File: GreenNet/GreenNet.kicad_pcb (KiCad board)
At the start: 2 copper layers, 32 parts, among them U1 ESP32-S3-WROOM-1-N16R2, U2 USB_C_Receptacle_12P, U3 USB_C_Receptacle_12P, U4 CP2102N-A02-GQFN28

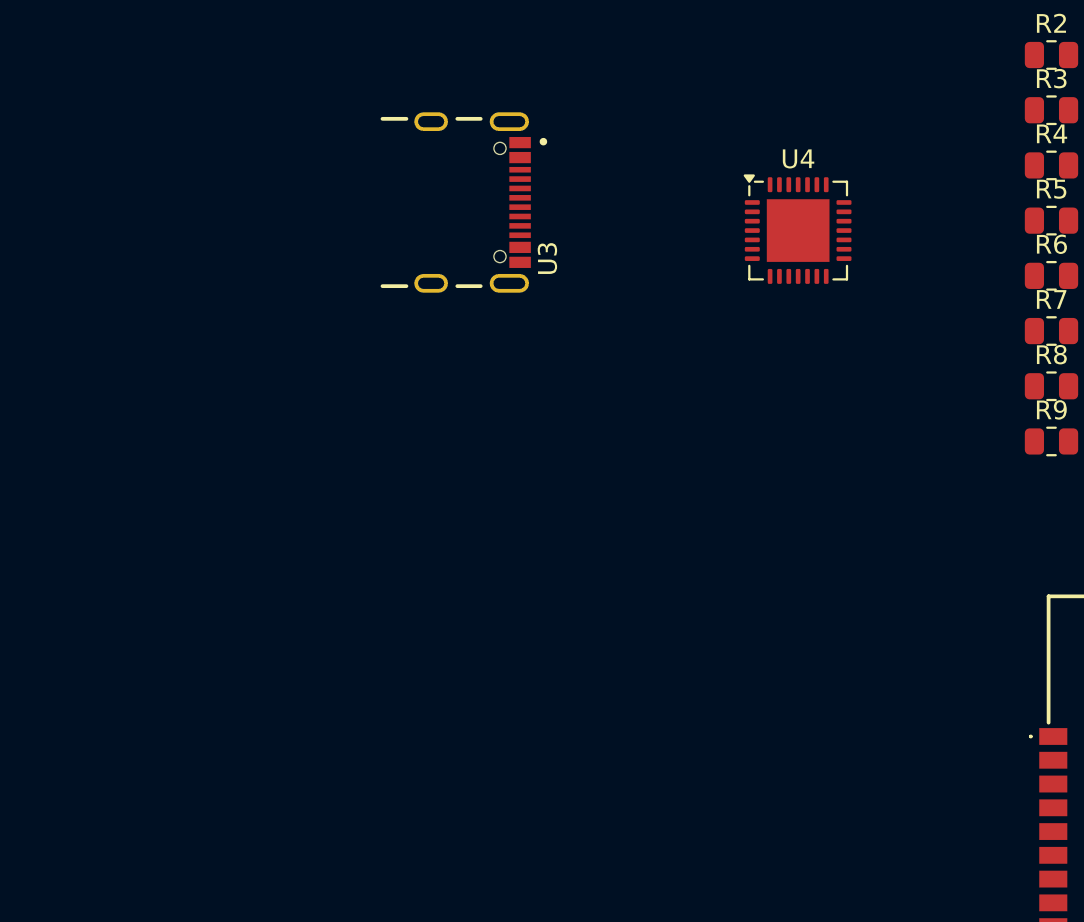
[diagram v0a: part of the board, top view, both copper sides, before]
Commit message: finished input schematic
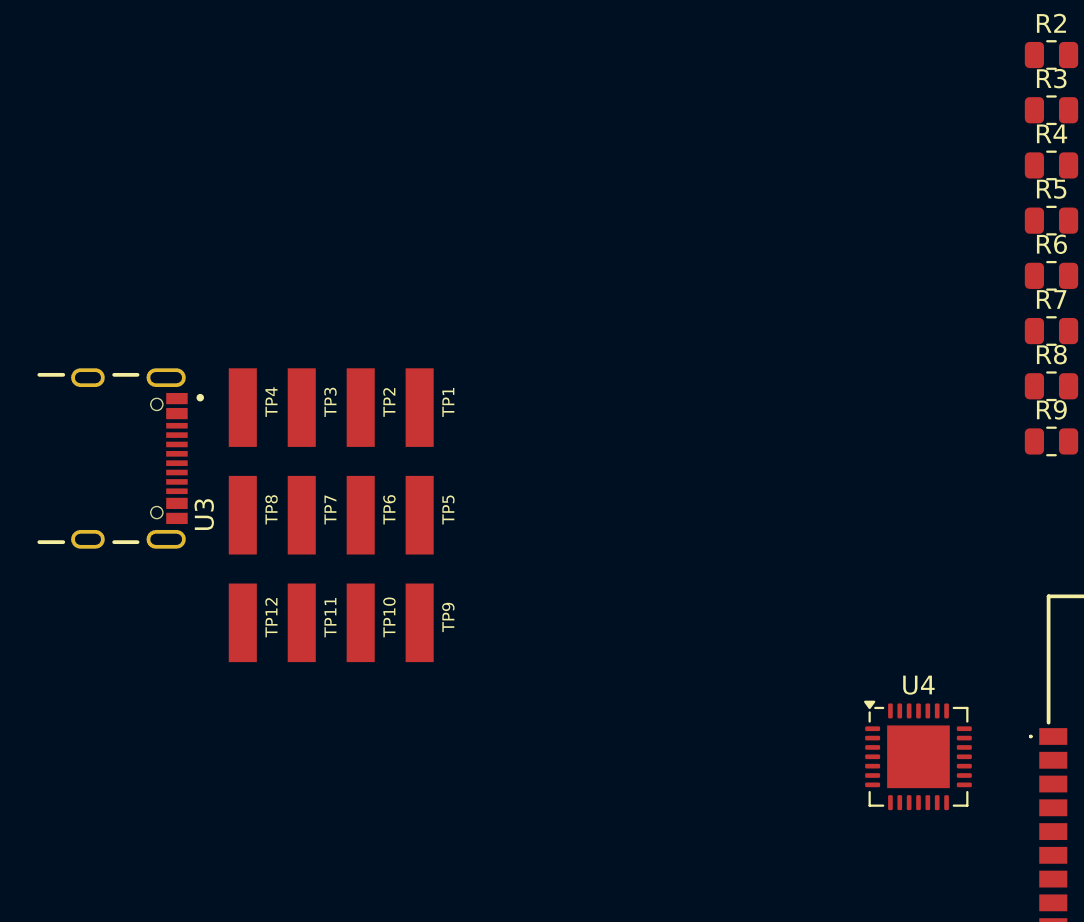
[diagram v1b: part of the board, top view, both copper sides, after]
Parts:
- added TP1: TestPoint, AA_TestPoints:RCWCTE, F.Cu at (103.2, 83.5)
- added TP10: TestPoint, AA_TestPoints:RCWCTE, F.Cu at (100.1, 95.0)
- added TP11: TestPoint, AA_TestPoints:RCWCTE, F.Cu at (96.9, 95.0)
- added TP12: TestPoint, AA_TestPoints:RCWCTE, F.Cu at (93.8, 95.0)
- added TP2: TestPoint, AA_TestPoints:RCWCTE, F.Cu at (100.1, 83.5)
- added TP3: TestPoint, AA_TestPoints:RCWCTE, F.Cu at (96.9, 83.5)
- added TP4: TestPoint, AA_TestPoints:RCWCTE, F.Cu at (93.8, 83.5)
- added TP5: TestPoint, AA_TestPoints:RCWCTE, F.Cu at (103.2, 89.2)
- added TP6: TestPoint, AA_TestPoints:RCWCTE, F.Cu at (100.1, 89.2)
- added TP7: TestPoint, AA_TestPoints:RCWCTE, F.Cu at (96.9, 89.2)
- added TP8: TestPoint, AA_TestPoints:RCWCTE, F.Cu at (93.8, 89.2)
- added TP9: TestPoint, AA_TestPoints:RCWCTE, F.Cu at (103.2, 95.0)
- moved U4 28.8 mm to (129.9, 102.1)
- moved U3 22.9 mm to (85.5, 86.2)
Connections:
- D3 pad 3: /Input/USB_UART_D+ -> /Input/USB_UART_D-
- U3 pad A7: /Input/USB_UART_D+ -> /Input/USB_UART_D-
- U3 pad B7: /Input/USB_UART_D+ -> /Input/USB_UART_D-
- U4 pad 5: /Input/USB_UART_D+ -> /Input/USB_UART_D-

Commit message: MCU fix
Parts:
- added R10: 10k, Resistor_SMD:R_0805_2012Metric, F.Cu at (127.1, 105.5)
- added R11: 10k, Resistor_SMD:R_0805_2012Metric, F.Cu at (127.1, 108.5)
- added U5: MC33063AD, Package_SO:SOIC-8_3.9x4.9mm_P1.27mm, F.Cu at (129.1, 98.8)
- moved R7 73.9 mm to (204.9, 108.5)
- moved D1 68.4 mm to (91.0, 49.1)
- moved D3 67.1 mm to (90.5, 65.1)
- moved U4 66.1 mm to (196.0, 100.5)
- moved D7 63.5 mm to (101.9, 48.6)
- moved C10 58.7 mm to (90.5, 53.6)
- moved D2 58.0 mm to (97.0, 54.6)
- moved R6 56.8 mm to (187.9, 101.5)
- moved D5 55.2 mm to (200.1, 108.5)
- moved D6 55.2 mm to (102.6, 68.1)
- moved U1 54.6 mm to (138.2, 52.3)
- moved D4 51.7 mm to (97.5, 71.6)
- moved C9 51.5 mm to (90.9, 69.6)
- moved C4 51.0 mm to (182.1, 95.5)
- moved C5 51.0 mm to (182.1, 98.5)
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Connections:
- U1 pad 27: unconnected-(U1-IO0-Pad27) -> /Microcontroller/S3_BOOT
- U1 pad 36: unconnected-(U1-RXD0-Pad36) -> /Input/UART_TXD
- U1 pad 37: unconnected-(U1-TXD0-Pad37) -> /Input/UART_RXD
- U1 pad 42: (no net) -> GND
- U1 pad 43: (no net) -> GND
- U1 pad 44: (no net) -> GND
- U1 pad 45: (no net) -> GND
- U1 pad 46: (no net) -> GND
- U1 pad 47: (no net) -> GND
- U1 pad 48: (no net) -> GND
- U1 pad 49: (no net) -> GND
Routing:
- added copper zone on F.Cu, net GND
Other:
- copper layers 2 -> 4

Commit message: USB-PC PD progress
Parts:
- removed R2, R3: 5.1k, Resistor_SMD:R_0805_2012Metric
- removed TP1, TP10, TP11, TP12, TP2, TP3, TP4, TP5, TP6, TP7, TP8, TP9: TestPoint, AA_TestPoints:RCWCTE
- added IC1: BQ24250RGET, QFN:QFN50P400X400X100-25N-D, F.Cu at (132.5, 102.8)
- added Q4: IRF9358TRPBF, AA_FETS:SO8_IRF9358TRPBF_INF, F.Cu at (122.0, 75.6)
- added TP13: TestPoint, AA_TestPoints:RCWCTE, F.Cu at (107.3, 61.2)
- added TP14: TestPoint, AA_TestPoints:RCWCTE, F.Cu at (107.3, 64.4)
- added TP15: TestPoint, AA_TestPoints:RCWCTE, F.Cu at (107.3, 67.5)
- added TP16: TestPoint, AA_TestPoints:RCWCTE, F.Cu at (107.3, 70.7)
- added TP17: TestPoint, AA_TestPoints:RCWCTE, F.Cu at (113.0, 61.2)
- added TP18: TestPoint, AA_TestPoints:RCWCTE, F.Cu at (113.0, 64.4)
- added TP19: TestPoint, AA_TestPoints:RCWCTE, F.Cu at (113.0, 67.5)
- added TP20: TestPoint, AA_TestPoints:RCWCTE, F.Cu at (113.0, 70.7)
- added TP21: TestPoint, AA_TestPoints:RCWCTE, F.Cu at (118.8, 61.2)
- added TP22: TestPoint, AA_TestPoints:RCWCTE, F.Cu at (118.8, 64.4)
- added TP23: TestPoint, AA_TestPoints:RCWCTE, F.Cu at (118.8, 67.5)
- added TP24: TestPoint, AA_TestPoints:RCWCTE, F.Cu at (118.8, 70.7)
- added U6: CYPD3177-24LQXQT, AA_Interface_USB:QFN50P400X400X60-25N-D, F.Cu at (121.2, 89.3)
- moved R7 97.4 mm to (111.0, 82.6)
- moved D8 95.1 mm to (115.5, 82.9)
- moved D9 95.1 mm to (115.5, 86.0)
- moved D5 91.5 mm to (115.5, 73.8)
- moved R6 79.9 mm to (111.0, 79.6)
- moved C4 78.5 mm to (106.6, 73.8)
- moved C5 78.5 mm to (106.6, 76.8)
- moved C6 78.5 mm to (106.6, 79.8)
- moved C7 78.5 mm to (106.6, 82.8)
- moved C8 78.5 mm to (106.6, 85.8)
- moved U4 78.0 mm to (118.0, 99.5)
- moved C10 41.5 mm to (106.6, 91.8)
- moved R10 41.2 mm to (152.6, 73.1)
- moved R11 41.2 mm to (152.6, 76.1)
- moved R9 37.2 mm to (111.0, 88.5)
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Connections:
- R6 pad 1: VDD -> /Input/UART_VDD
- U2 pad A5: Net-(U2-CC1) -> /Input/USB_CC1
- U2 pad B5: Net-(U2-CC2) -> /Input/USB_CC2
- U4 pad 6: VDD -> /Input/UART_VDD
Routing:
- removed copper zone on F.Cu, net GND

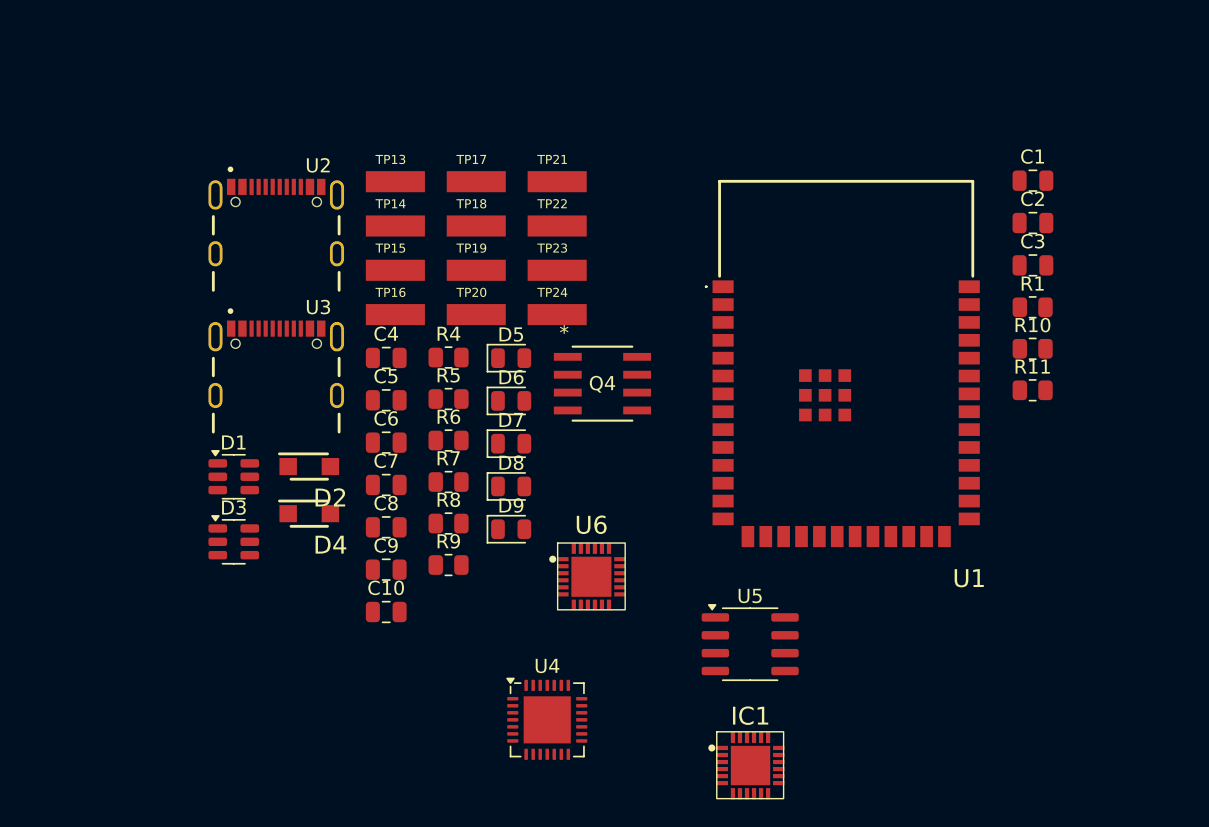
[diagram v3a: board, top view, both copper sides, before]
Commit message: input schematic finished
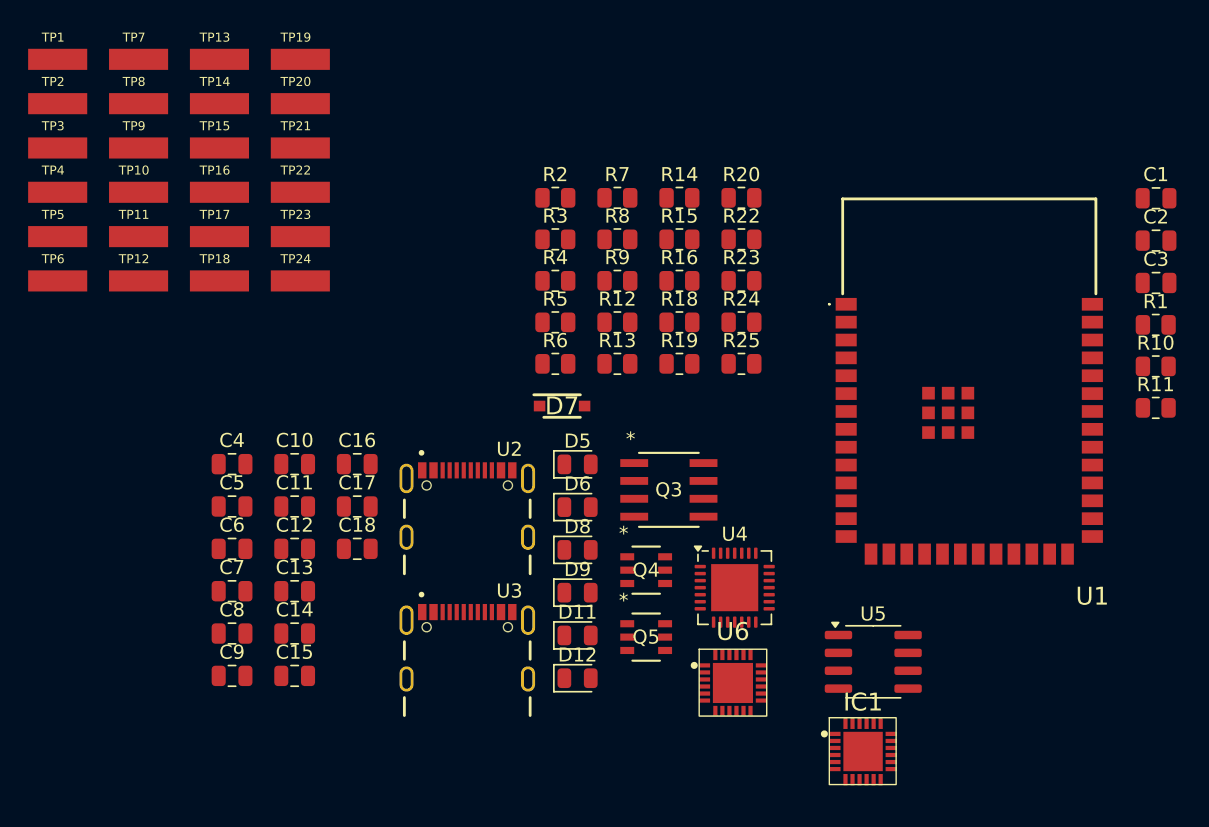
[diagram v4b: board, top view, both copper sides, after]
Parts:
- removed D1, D3: ESDA6V1BC6, Package_TO_SOT_SMD:SOT-23-6
- removed D2, D4: DSS14U, AA_Diodes:SOD-123FL
- added C11: 1u, Capacitor_SMD:C_0805_2012Metric, F.Cu at (100.1, 84.3)
- added C12: 1u, Capacitor_SMD:C_0805_2012Metric, F.Cu at (100.1, 87.3)
- added C13: 0.1u, Capacitor_SMD:C_0805_2012Metric, F.Cu at (100.1, 90.4)
- added C14: 0.1u, Capacitor_SMD:C_0805_2012Metric, F.Cu at (100.1, 93.4)
- added C15: 390p, Capacitor_SMD:C_0805_2012Metric, F.Cu at (100.1, 96.4)
- added C16: 390p, Capacitor_SMD:C_0805_2012Metric, F.Cu at (104.5, 81.3)
- added C17: 1u, Capacitor_SMD:C_0805_2012Metric, F.Cu at (104.5, 84.3)
- added C18: 1u, Capacitor_SMD:C_0805_2012Metric, F.Cu at (104.5, 87.3)
- added D11: Green, LED_SMD:LED_0805_2012Metric, F.Cu at (120.2, 93.5)
- added D12: Red, LED_SMD:LED_0805_2012Metric, F.Cu at (120.2, 96.5)
- added Q3: IRF9358TRPBF, AA_FETS:SO8_IRF9358TRPBF_INF, F.Cu at (126.7, 83.2)
- added Q5: SI3993CDV-T1-GE3, AA_FETS:TSOP_0DV-T1-E3_VIS, F.Cu at (125.1, 93.6)
- added R12: 49.9k, Resistor_SMD:R_0805_2012Metric, F.Cu at (123.0, 71.2)
- added R13: 1k, Resistor_SMD:R_0805_2012Metric, F.Cu at (123.0, 74.2)
- added R14: 49.9k, Resistor_SMD:R_0805_2012Metric, F.Cu at (127.4, 62.4)
- added R15: 62R, Resistor_SMD:R_0805_2012Metric, F.Cu at (127.4, 65.3)
- added R16: 49.9k, Resistor_SMD:R_0805_2012Metric, F.Cu at (127.4, 68.3)
- added R18: 62R, Resistor_SMD:R_0805_2012Metric, F.Cu at (127.4, 71.2)
- added R19: 62R, Resistor_SMD:R_0805_2012Metric, F.Cu at (127.4, 74.2)
- added R2: 1k, Resistor_SMD:R_0805_2012Metric, F.Cu at (118.6, 62.4)
- added R20: 62R, Resistor_SMD:R_0805_2012Metric, F.Cu at (131.9, 62.4)
- added R22: 5.1k, Resistor_SMD:R_0805_2012Metric, F.Cu at (131.9, 65.3)
- added R23: 1k, Resistor_SMD:R_0805_2012Metric, F.Cu at (131.9, 68.3)
- added R24: 5.1k, Resistor_SMD:R_0805_2012Metric, F.Cu at (131.9, 71.2)
- added R25: 2.4k, Resistor_SMD:R_0805_2012Metric, F.Cu at (131.9, 74.2)
- added R3: 10k, Resistor_SMD:R_0805_2012Metric, F.Cu at (118.6, 65.3)
- added TP1: TestPoint, AA_TestPoints:RCWCTE, F.Cu at (83.2, 52.5)
- added TP10: TestPoint, AA_TestPoints:RCWCTE, F.Cu at (89.0, 62.0)
- added TP11: TestPoint, AA_TestPoints:RCWCTE, F.Cu at (89.0, 65.2)
- added TP12: TestPoint, AA_TestPoints:RCWCTE, F.Cu at (89.0, 68.3)
- added TP2: TestPoint, AA_TestPoints:RCWCTE, F.Cu at (83.2, 55.7)
- added TP3: TestPoint, AA_TestPoints:RCWCTE, F.Cu at (83.2, 58.9)
- added TP4: TestPoint, AA_TestPoints:RCWCTE, F.Cu at (83.2, 62.0)
- added TP5: TestPoint, AA_TestPoints:RCWCTE, F.Cu at (83.2, 65.2)
- added TP6: TestPoint, AA_TestPoints:RCWCTE, F.Cu at (83.2, 68.3)
- added TP7: TestPoint, AA_TestPoints:RCWCTE, F.Cu at (89.0, 52.5)
- added TP8: TestPoint, AA_TestPoints:RCWCTE, F.Cu at (89.0, 55.7)
- added TP9: TestPoint, AA_TestPoints:RCWCTE, F.Cu at (89.0, 58.9)
- D7: value Green -> 10V; footprint LED_SMD:LED_0805_2012Metric -> AA_Diodes:NHZ10C,115
- Q4: value IRF9358TRPBF -> SI3993CDV-T1-GE3; footprint AA_FETS:SO8_IRF9358TRPBF_INF -> AA_FETS:TSOP_0DV-T1-E3_VIS
- R7: value 43R -> 62R
- R9: value 62R -> 1k
- moved U3 24.3 mm to (112.4, 96.6)
- moved U2 24.3 mm to (112.4, 86.5)
- moved R8 23.5 mm to (123.0, 65.3)
- moved R9 23.5 mm to (123.0, 68.3)
- moved R7 23.5 mm to (123.0, 62.4)
- moved TP19 19.5 mm to (100.5, 52.5)
- moved TP20 19.5 mm to (100.5, 55.7)
- moved TP17 18.7 mm to (94.8, 65.2)
- moved TP18 18.7 mm to (94.8, 68.3)
- moved TP21 18.4 mm to (100.5, 58.9)
- moved TP22 18.4 mm to (100.5, 62.0)
- moved TP23 18.4 mm to (100.5, 65.2)
- moved TP24 18.4 mm to (100.5, 68.3)
- moved U4 16.3 mm to (131.4, 90.1)
- moved TP13 15.2 mm to (94.8, 52.5)
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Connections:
- C4 pad 1: VDD -> /Input/UART_VDD
- C5 pad 1: VDD -> /Input/UART_VDD
- D7 pad 1: GND -> /Input/FET_SRC
- D7 pad 2: Net-(D7-A) -> /Input/FET_GATE
- D8 pad 2: VDD -> Net-(D8-A)
- D9 pad 2: VDD -> Net-(D9-A)
- Q4 pad 2: unconnected-(Q4-G2-Pad2) -> Net-(Q4-S1)
- Q4 pad 4: unconnected-(Q4-G1-Pad4) -> VUART
- Q4 pad 5: Net-(Q4-D1-Pad5) -> Net-(Q4-S1)
- Q4 pad 6: Net-(Q4-D1-Pad5) -> VBUS
- R7 pad 1: VDD -> /Input/UART_VDD
- R9 pad 1: VUSB -> /Input/FET_GATE
- R9 pad 2: Net-(D7-A) -> /Input/VBUS_FET_EN
- TP14 pad 1: VBUS -> VUART
- TP16 pad 1: VUART -> VBUS
- U6 pad 1: /Input/VBUS_MIN -> GND
- U6 pad 10: /Input/USB_FLIP -> unconnected-(U6-FLIP-Pad10)
- U6 pad 11: /Input/USB_VDC_OUT -> VBUS
- U6 pad 6: /Input/ISINK_FINE -> GND

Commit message: started layout
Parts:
- removed TP1, TP10, TP11, TP12, TP13, TP14, TP15, TP16, TP17, TP18, TP19, TP2, TP20, TP21, TP22, TP23, TP24, TP3, TP4, TP5, TP6, TP7, TP8, TP9: TestPoint, AA_TestPoints:RCWCTE
- added D1: D5V0M1U2S9, AA_Diodes:D5V0M1U2S9Q, F.Cu at (79.8, 85.5)
- added D10: D5V0M1U2S9, AA_Diodes:D5V0M1U2S9Q, F.Cu at (79.8, 83.0)
- added D2: D5V0M1U2S9, AA_Diodes:D5V0M1U2S9Q, F.Cu at (82.8, 61.0)
- added D3: D5V0M1U2S9, AA_Diodes:D5V0M1U2S9Q, F.Cu at (82.8, 63.0)
- added D4: D5V0M1U2S9, AA_Diodes:D5V0M1U2S9Q, F.Cu at (82.8, 65.0)
- C15, C16, R4, R5: moved to B.Cu
- Q4: value SI3993CDV-T1-GE3 -> SI3932DV-T1-GE3
- U4: value CP2102N-A02-GQFN28 -> CP2102N
- moved U1 86.6 mm to (228.2, 42.5)
- moved U5 79.7 mm to (215.7, 123.6)
- moved IC1 70.3 mm to (209.2, 87.0)
- moved D11 60.4 mm to (89.8, 41.2)
- moved D12 55.2 mm to (137.2, 44.0)
- moved R4 55.0 mm to (72.0, 97.5)
- moved C14 53.6 mm to (124.7, 45.7)
- moved R5 52.0 mm to (72.1, 94.5)
- moved U4 49.7 mm to (82.0, 95.5)
- moved C18 49.7 mm to (124.8, 42.0)
- moved C17 49.7 mm to (124.8, 39.0)
- moved Q5 48.8 mm to (102.3, 50.4)
- moved C13 48.4 mm to (118.8, 45.7)
- moved Q3 47.7 mm to (108.0, 39.2), turned to 90 degrees
- moved R15 47.2 mm to (89.7, 37.0)
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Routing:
- net GND: track 0.00 -> 10.3 mm, vias 0 -> 31
- net /Input/USB_D-: track 0.00 -> 7.73 mm
- net /Input/UART_VDD: track 0.00 -> 7.26 mm, vias 0 -> 2
- net /Input/USB_D+: track 0.00 -> 7.18 mm
- net /Input/USB_UART_D+: track 0.00 -> 6.76 mm, vias 0 -> 2
- net /Input/USB_UART_D-: track 0.00 -> 6.64 mm
- net Net-(U3-CC2): track 0.00 -> 2.84 mm, vias 0 -> 1
- net Net-(U3-CC1): track 0.00 -> 2.84 mm, vias 0 -> 1
- net /Input/USB_CC2: track 0.00 -> 2.84 mm, vias 0 -> 1
- net /Input/USB_CC1: track 0.00 -> 2.84 mm, vias 0 -> 1
- net Net-(U4-~{RST}): track 0.00 -> 1.90 mm
- net VUART: track 0.00 -> 1.34 mm, vias 0 -> 16
- net VUSB: vias 0 -> 16
- added copper zone on F.Cu, net GND
- added copper zone on In1.Cu, net GND
- added copper zone on In2.Cu, net GND
- added copper zone on F.Cu, net VUART
- added copper zone on F.Cu, net VUSB
- added copper zone on In1.Cu, net VUSB

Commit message: more sensor work
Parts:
- removed IC1: BQ24250RGET, QFN:QFN50P400X400X100-25N-D
- added C19: 1u, Capacitor_SMD:C_0805_2012Metric, F.Cu at (134.8, 69.4)
- added C20: 1u, Capacitor_SMD:C_0805_2012Metric, F.Cu at (134.8, 72.4)
- added C23: 10p, Capacitor_SMD:C_0805_2012Metric, F.Cu at (210.2, 90.0)
- added C24: 10p, Capacitor_SMD:C_0805_2012Metric, F.Cu at (210.2, 93.1)
- added C25: 10p, Capacitor_SMD:C_0805_2012Metric, F.Cu at (210.2, 96.1)
- added C26: 1u, Capacitor_SMD:C_0805_2012Metric, F.Cu at (210.2, 99.1)
- added C27: 0.1u, Capacitor_SMD:C_0805_2012Metric, F.Cu at (210.2, 102.1)
- added C28: 0.1u, Capacitor_SMD:C_0805_2012Metric, F.Cu at (210.2, 105.1)
- added IC5: BQ24250RGER, QFN:QFN50P400X400X100-25N-D, F.Cu at (211.5, 111.8)
- added IC6: NCP186AMX330TAG, AA_Power_ICs:NCP186AMX330TAG, F.Cu at (210.3, 117.4)
- added TP1: TestPoint, AA_TestPoints:RCWCTE, F.Cu at (191.6, 90.1)
- added TP10: TestPoint, AA_TestPoints:RCWCTE, F.Cu at (191.6, 112.2)
- added TP11: TestPoint, AA_TestPoints:RCWCTE, F.Cu at (197.4, 90.1)
- added TP12: TestPoint, AA_TestPoints:RCWCTE, F.Cu at (197.4, 93.3)
- added TP13: TestPoint, AA_TestPoints:RCWCTE, F.Cu at (197.4, 96.4)
- added TP14: TestPoint, AA_TestPoints:RCWCTE, F.Cu at (197.4, 99.6)
- added TP15: TestPoint, AA_TestPoints:RCWCTE, F.Cu at (197.4, 102.7)
- added TP16: TestPoint, AA_TestPoints:RCWCTE, F.Cu at (197.4, 105.9)
- added TP17: TestPoint, AA_TestPoints:RCWCTE, F.Cu at (197.4, 109.0)
- added TP18: TestPoint, AA_TestPoints:RCWCTE, F.Cu at (197.4, 112.2)
- added TP19: TestPoint, AA_TestPoints:RCWCTE, F.Cu at (203.1, 90.1)
- added TP2: TestPoint, AA_TestPoints:RCWCTE, F.Cu at (191.6, 93.3)
- added TP20: TestPoint, AA_TestPoints:RCWCTE, F.Cu at (203.1, 93.3)
- added TP21: TestPoint, AA_TestPoints:RCWCTE, F.Cu at (203.1, 96.4)
- added TP22: TestPoint, AA_TestPoints:RCWCTE, F.Cu at (203.1, 99.6)
- added TP23: TestPoint, AA_TestPoints:RCWCTE, F.Cu at (203.1, 102.7)
- added TP24: TestPoint, AA_TestPoints:RCWCTE, F.Cu at (203.1, 105.9)
- added TP4: TestPoint, AA_TestPoints:RCWCTE, F.Cu at (191.6, 96.4)
- added TP6: TestPoint, AA_TestPoints:RCWCTE, F.Cu at (191.6, 99.6)
- added TP7: TestPoint, AA_TestPoints:RCWCTE, F.Cu at (191.6, 102.7)
- added TP8: TestPoint, AA_TestPoints:RCWCTE, F.Cu at (191.6, 105.9)
- added TP9: TestPoint, AA_TestPoints:RCWCTE, F.Cu at (191.6, 109.0)
- added U7: LTR-303ALS-01, OptoDevice:Lite-On_LTR-303ALS-01, F.Cu at (214.5, 94.8)
- C10, C9: value 22u -> 10u
- U4: value CP2102N -> CP2102N-A02-GQFN28
- U5: value MC33063AD -> BME280; footprint Package_SO:SOIC-8_3.9x4.9mm_P1.27mm -> Package_LGA:Bosch_LGA-8_2.5x2.5mm_P0.65mm_ClockwisePinNumbering
- moved U5 32.8 mm to (214.7, 90.8)
- moved U4 4.50 mm to (86.5, 95.5)
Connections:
- U5 pad 1: unconnected-(U5-SwC-Pad1) -> GND
- U5 pad 2: unconnected-(U5-SwE-Pad2) -> +3.3V
- U5 pad 3: unconnected-(U5-TC-Pad3) -> /Sensors/SENSOR_SDA
- U5 pad 4: GND -> /Sensors/SENSOR_SCL
- U5 pad 5: unconnected-(U5-Vfb-Pad5) -> GND
- U5 pad 6: unconnected-(U5-Vin-Pad6) -> +3.3V
- U5 pad 7: unconnected-(U5-Ipk-Pad7) -> GND
- U5 pad 8: unconnected-(U5-DC-Pad8) -> +3.3V
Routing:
- net /Input/UART_VDD: track 7.26 -> 5.40 mm, vias 2 -> 1
- net Net-(U4-~{RST}): track 1.90 -> 0.35 mm
- net VUART: track 1.34 -> 0.00 mm
- added copper zone on B.Cu, net VUSB
